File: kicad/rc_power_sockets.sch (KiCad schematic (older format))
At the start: 14 parts

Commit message: Schematic
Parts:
- removed J?: SIL6, symbol SIL6
- added JP?: Jumper_NO_Small, symbol Jumper_NO_Small
- added P?: ICSP, symbol DIL6
- J?: value SIL3 -> Motion Sensor
- J?: value SIL3 -> Radio 433MHZ
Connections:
- net labels added: DATA, MISO, MOSI, RESET, SCK
- net labels removed: MOTION
- wire segments 17 -> 38
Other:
- moved on the sheet: C?, D?, IC?, J?, Q?, R?, SW?, U?

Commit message: Schematic
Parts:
- removed J?: Motion Sensor, symbol SIL3
- removed J?: Radio 433MHZ, symbol SIL3
- added P?: DIL6, symbol DIL6
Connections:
- net labels added: POWER, POWER_SWITCHED, RADIO_DATA
- net labels removed: BATTERY, DATA
- wire segments 38 -> 45
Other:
- moved on the sheet: C?, D?, IC?, JP?, P?, Q?, R?, SW?, U?

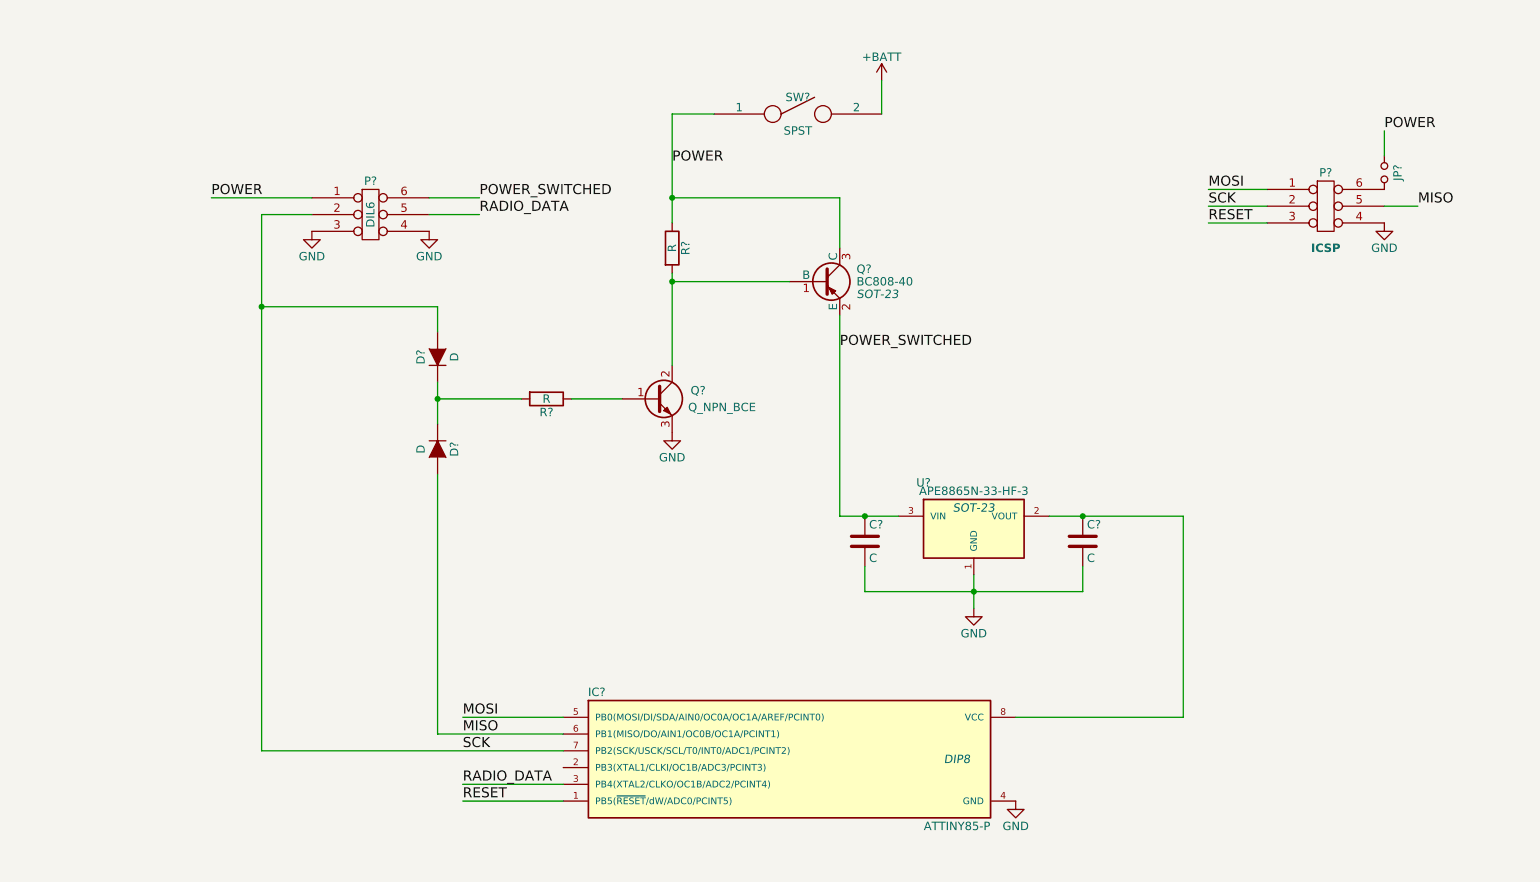
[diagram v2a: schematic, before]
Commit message: SIL for sensors
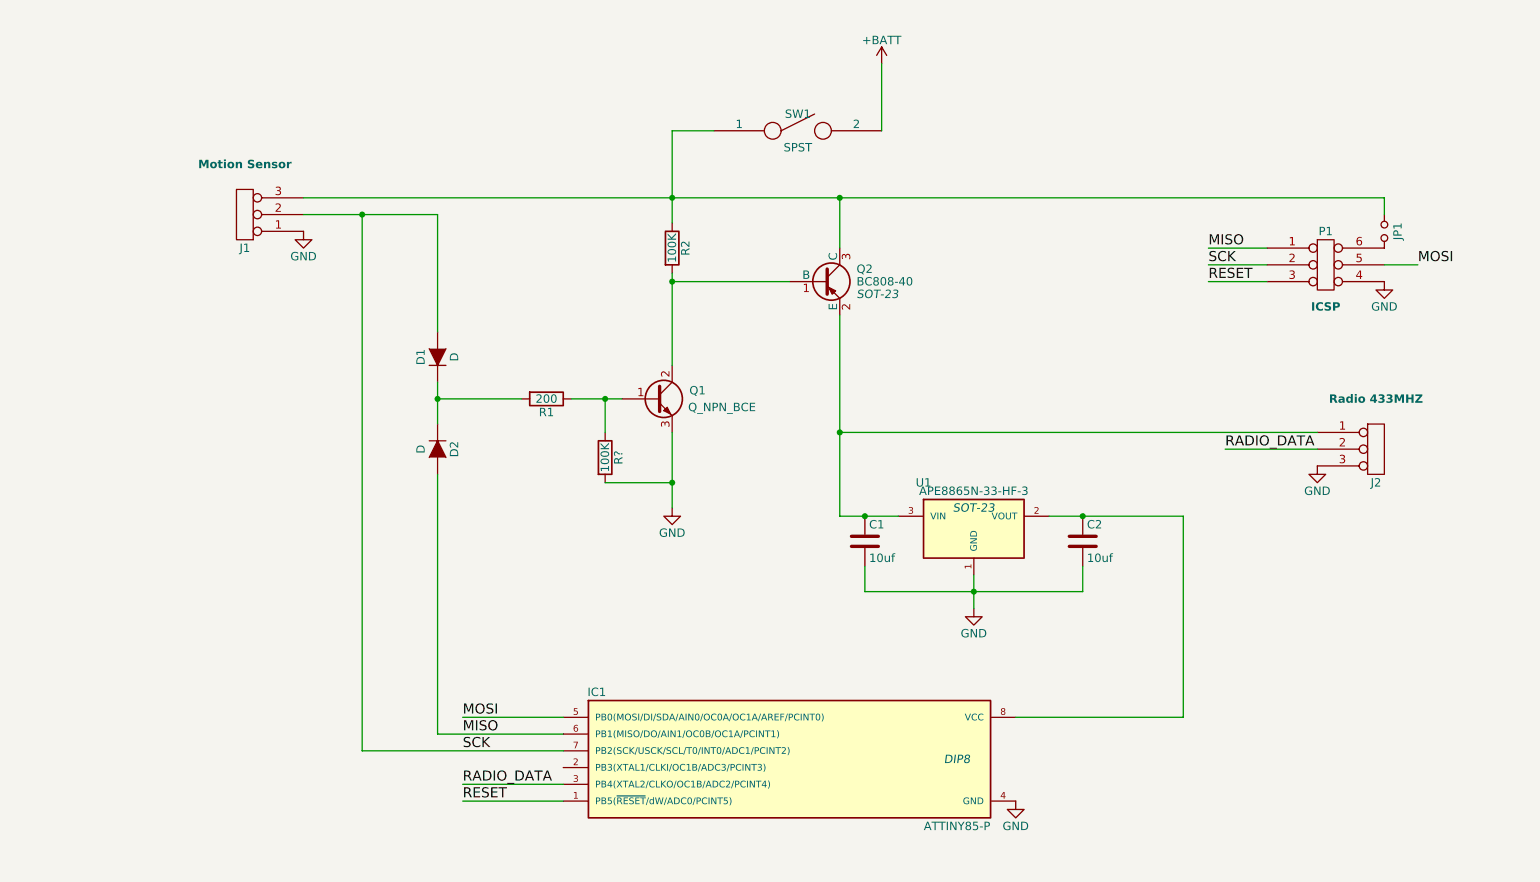
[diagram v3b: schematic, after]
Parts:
- removed P?: DIL6, symbol DIL6
- added J1: Motion Sensor, symbol SIL3
- added J2: Radio 433MHZ, symbol SIL3
- added R?: 100K, symbol R
- C1, C2: renamed from C?; value C -> 10uf
- R1: renamed from R?; value R -> 200
- R2: renamed from R?; value R -> 100K
- gave numbers to parts that had none: 9
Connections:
- net GND: now also J1.1, J2.3, R?.2
- net MISO: now also P1.1 (P1); no longer P1.5 (P5)
- net MOSI: now also P1.5 (P5); no longer P1.1 (P1)
- net RADIO_DATA: now also J2.2
- net SCK: now also J1.2
- net at Q1.1 (B), R1.1: now also R?.1
- net POWER: no longer names the net of JP1.1, Q2.3 (C), R2.1, SW1.1
- net POWER: now also J1.3
- net POWER_SWITCHED: no longer names the net of C1.1, Q2.2 (E), U1.3 (VIN)
- net POWER_SWITCHED: now also J2.1
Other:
- moved on the sheet: JP1, P1, SW1

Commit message: Annotate
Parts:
- added R4: 100K, symbol R
- gave numbers to parts that had none: 1
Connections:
- net RESET: now also R4.1
- net at C2.1, IC1.8 (VCC), U1.2 (VOUT): now also R4.2
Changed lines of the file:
@@
 $EndComp
 $Comp
-L +BATT #PWR3
+L +BATT #PWR01
 U 1 1 56D4AEA2
 P 6800 1150
-F 0 "#PWR3" H 6800 1000 50  0001 C CNN
+F 0 "#PWR01" H 6800 1000 50  0001 C CNN
 F 1 "+BATT" H 6800 1290 50  0000 C CNN
 F 2 "" H 6800 1150 50  0000 C CNN
@@
 $EndComp
 $Comp
-L GND #PWR4
+L GND #PWR02
 U 1 1 56D4B298
 P 7350 4400
-F 0 "#PWR4" H 7350 4150 50  0001 C CNN
+F 0 "#PWR02" H 7350 4150 50  0001 C CNN
 F 1 "GND" H 7350 4250 50  0000 C CNN
 F 2 "" H 7350 4400 50  0000 C CNN
@@
 $EndComp
 $Comp
-L GND #PWR2
+L GND #PWR03
 U 1 1 56D4D563
 P 5550 3800
-F 0 "#PWR2" H 5550 3550 50  0001 C CNN
+F 0 "#PWR03" H 5550 3550 50  0001 C CNN
 F 1 "GND" H 5550 3650 50  0000 C CNN
 F 2 "" H 5550 3800 50  0000 C CNN
@@
 $EndComp
 $Comp
-L GND #PWR5
+L GND #PWR04
 U 1 1 56D4E393
 P 7600 5550
-F 0 "#PWR5" H 7600 5300 50  0001 C CNN
+F 0 "#PWR04" H 7600 5300 50  0001 C CNN
 F 1 "GND" H 7600 5400 50  0000 C CNN
 F 2 "" H 7600 5550 50  0000 C CNN
@@
 SCK
 $Comp
-L GND #PWR7
+L GND #PWR05
 U 1 1 56D7102B
 P 9800 2450
-F 0 "#PWR7" H 9800 2200 50  0001 C CNN
+F 0 "#PWR05" H 9800 2200 50  0001 C CNN
 F 1 "GND" H 9800 2300 50  0000 C CNN
 F 2 "" H 9800 2450 50  0000 C CNN
@@
 RADIO_DATA
 $Comp
-L GND #PWR6
+L GND #PWR06
 U 1 1 56D83AA4
 P 9400 3550
-F 0 "#PWR6" H 9400 3300 50  0001 C CNN
+F 0 "#PWR06" H 9400 3300 50  0001 C CNN
 F 1 "GND" H 9400 3400 50  0000 C CNN
 F 2 "" H 9400 3550 50  0000 C CNN
@@
 $EndComp
 $Comp
-L GND #PWR1
+L GND #PWR07
 U 1 1 56D83C01
 P 3350 2150
-F 0 "#PWR1" H 3350 1900 50  0001 C CNN
+F 0 "#PWR07" H 3350 1900 50  0001 C CNN
 F 1 "GND" H 3350 2000 50  0000 C CNN
 F 2 "" H 3350 2150 50  0000 C CNN
@@
 	8000 4300 8000 4150
 Wire Wire Line
-	8600 3850 8600 5050
+	8600 3850 8600 5950
 Wire Wire Line
 	8600 5050 7600 5050
@@
 	5550 3350 5550 3800
 $Comp
-L R R?
+L R R3
 U 1 1 56D8549B
 P 5150 3500
-F 0 "R?" V 5230 3500 50  0000 C CNN
+F 0 "R3" V 5230 3500 50  0000 C CNN
 F 1 "100K" V 5150 3500 50  0000 C CNN
 F 2 "" V 5080 3500 50  0000 C CNN
@@
 	5150 3350 5150 3150
 Connection ~ 5150 3150
+$Comp
+L R R4
+U 1 1 56D85890
+P 4750 5800
+F 0 "R4" V 4830 5800 50  0000 C CNN
+F 1 "100K" V 4750 5800 50  0000 C CNN
+F 2 "" V 4680 5800 50  0000 C CNN
+F 3 "" H 4750 5800 50  0000 C CNN
+	1    4750 5800
+	1    0    0    -1
+$EndComp
+Wire Wire Line
+	4750 5650 4750 5550
+Connection ~ 4750 5550
+Wire Wire Line
+	8600 5950 4750 5950
+Connection ~ 8600 5050
 $EndSCHEMATC

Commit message: Footprints
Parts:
- C1, C2: footprint (none) -> Capacitors_SMD:C_1206_HandSoldering
- D1, D2: footprint (none) -> SMD_Packages:SMD-1206_Pol
- IC1: footprint DIP8 -> Housings_DIP:DIP-8_W7.62mm_LongPads
- J1, J2: footprint (none) -> Pin_Headers:Pin_Header_Straight_1x03
- JP1: footprint (none) -> Pin_Headers:Pin_Header_Straight_1x02
- P1: footprint (none) -> Pin_Headers:Pin_Header_Straight_2x03
- Q1: footprint (none) -> TO_SOT_Packages_SMD:SOT-23_Handsoldering
- Q2, U1: footprint SOT-23 -> TO_SOT_Packages_SMD:SOT-23_Handsoldering
- R1, R2, R3, R4: footprint (none) -> Resistors_SMD:R_1206_HandSoldering
- SW1: footprint (none) -> Wire_Pads:SolderWirePad_2x_2-5mmDrill
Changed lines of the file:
@@
 F 0 "IC1" H 5100 5700 50  0000 C CNN
 F 1 "ATTINY85-P" H 7250 4900 50  0000 C CNN
-F 2 "DIP8" H 7250 5300 50  0000 C CIN
+F 2 "Housings_DIP:DIP-8_W7.62mm_LongPads" H 7250 5300 50  0000 C CIN
 F 3 "" H 6250 5300 50  0000 C CNN
 	1    6250 5300
@@
 F 0 "Q2" H 6650 2525 50  0000 L CNN
 F 1 "BC808-40" H 6650 2450 50  0000 L CNN
-F 2 "SOT-23" H 6650 2375 50  0000 L CIN
+F 2 "TO_SOT_Packages_SMD:SOT-23_Handsoldering" H 6650 2375 50  0000 L CIN
 F 3 "" H 6450 2450 50  0000 L CNN
 	1    6450 2450
@@
 F 0 "Q1" H 5750 3200 50  0000 R CNN
 F 1 "Q_NPN_BCE" H 6050 3100 50  0000 R CNN
-F 2 "" H 5650 3250 50  0000 C CNN
+F 2 "TO_SOT_Packages_SMD:SOT-23_Handsoldering" H 5650 3250 50  0001 C CNN
 F 3 "" H 5450 3150 50  0000 C CNN
 	1    5450 3150
@@
 F 0 "SW1" H 6300 1650 50  0000 C CNN
 F 1 "SPST" H 6300 1450 50  0000 C CNN
-F 2 "" H 6300 1550 50  0000 C CNN
+F 2 "Wire_Pads:SolderWirePad_2x_2-5mmDrill" H 6300 1550 50  0001 C CNN
 F 3 "" H 6300 1550 50  0000 C CNN
 	1    6300 1550
@@
 F 0 "R1" V 4880 3150 50  0000 C CNN
 F 1 "200" V 4800 3150 50  0000 C CNN
-F 2 "" V 4730 3150 50  0000 C CNN
+F 2 "Resistors_SMD:R_1206_HandSoldering" V 4730 3150 50  0001 C CNN
 F 3 "" H 4800 3150 50  0000 C CNN
 	1    4800 3150
@@
 F 0 "R2" V 5630 2250 50  0000 C CNN
 F 1 "100K" V 5550 2250 50  0000 C CNN
-F 2 "" V 5480 2250 50  0000 C CNN
+F 2 "Resistors_SMD:R_1206_HandSoldering" V 5480 2250 50  0001 C CNN
 F 3 "" H 5550 2250 50  0000 C CNN
 	1    5550 2250
@@
 F 0 "C2" H 8025 4100 50  0000 L CNN
 F 1 "10uf" H 8025 3900 50  0000 L CNN
-F 2 "" H 8038 3850 50  0000 C CNN
+F 2 "Capacitors_SMD:C_1206_HandSoldering" H 8038 3850 50  0001 C CNN
 F 3 "" H 8000 4000 50  0000 C CNN
 	1    8000 4000
@@
 F 0 "U1" H 7050 4150 50  0000 C CNN
 F 1 "APE8865N-33-HF-3" H 7350 4100 50  0000 C CNN
-F 2 "SOT-23" H 7350 4000 50  0000 C CIN
+F 2 "TO_SOT_Packages_SMD:SOT-23_Handsoldering" H 7350 4000 50  0000 C CIN
 F 3 "" H 7350 3900 50  0000 C CNN
 	1    7350 3900
@@
 F 0 "C1" H 6725 4100 50  0000 L CNN
 F 1 "10uf" H 6725 3900 50  0000 L CNN
-F 2 "" H 6738 3850 50  0000 C CNN
+F 2 "Capacitors_SMD:C_1206_HandSoldering" H 6738 3850 50  0001 C CNN
 F 3 "" H 6700 4000 50  0000 C CNN
 	1    6700 4000
@@
 F 0 "D1" H 4150 3000 50  0000 C CNN
 F 1 "D" H 4150 2800 50  0000 C CNN
-F 2 "" H 4150 2900 50  0000 C CNN
+F 2 "SMD_Packages:SMD-1206_Pol" H 4150 2900 50  0001 C CNN
 F 3 "" H 4150 2900 50  0000 C CNN
 	1    4150 2900
@@
 F 0 "D2" H 4150 3550 50  0000 C CNN
 F 1 "D" H 4150 3350 50  0000 C CNN
-F 2 "" H 4150 3450 50  0000 C CNN
+F 2 "SMD_Packages:SMD-1206_Pol" H 4150 3450 50  0001 C CNN
 F 3 "" H 4150 3450 50  0000 C CNN
 	1    4150 3450
@@
 F 0 "P1" H 9450 2550 50  0000 C CNN
 F 1 "ICSP" H 9450 2100 50  0000 C CNB
-F 2 "" H 9450 2350 50  0000 C CNN
+F 2 "Pin_Headers:Pin_Header_Straight_2x03" H 9450 2350 50  0001 C CNN
 F 3 "" H 9450 2350 50  0000 C CNN
 	1    9450 2350
@@
 F 0 "JP1" H 9800 2230 50  0000 C CNN
 F 1 "Jumper_NO_Small" H 9810 2090 50  0001 C CNN
-F 2 "" H 9800 2150 50  0000 C CNN
+F 2 "Pin_Headers:Pin_Header_Straight_1x02" H 9800 2150 50  0001 C CNN
 F 3 "" H 9800 2150 50  0000 C CNN
 	1    9800 2150
@@
 F 0 "J1" H 3000 2250 50  0000 C CNN
 F 1 "Motion Sensor" H 3000 1750 50  0000 C CNB
-F 2 "" H 3050 2050 50  0000 C CNN
+F 2 "Pin_Headers:Pin_Header_Straight_1x03" H 3050 2050 50  0001 C CNN
 F 3 "" H 3050 2050 50  0000 C CNN
 	1    3000 2050
@@
 F 0 "J2" H 9750 3250 50  0000 C CNN
 F 1 "Radio 433MHZ" H 9750 3750 50  0000 C CNB
-F 2 "" H 9800 3450 50  0000 C CNN
+F 2 "Pin_Headers:Pin_Header_Straight_1x03" H 9800 3450 50  0001 C CNN
 F 3 "" H 9800 3450 50  0000 C CNN
 	1    9750 3450
@@
 F 0 "R3" V 5230 3500 50  0000 C CNN
 F 1 "100K" V 5150 3500 50  0000 C CNN
-F 2 "" V 5080 3500 50  0000 C CNN
+F 2 "Resistors_SMD:R_1206_HandSoldering" V 5080 3500 50  0001 C CNN
 F 3 "" H 5150 3500 50  0000 C CNN
 	1    5150 3500
@@
 F 0 "R4" V 4830 5800 50  0000 C CNN
 F 1 "100K" V 4750 5800 50  0000 C CNN
-F 2 "" V 4680 5800 50  0000 C CNN
+F 2 "Resistors_SMD:R_1206_HandSoldering" V 4680 5800 50  0001 C CNN
 F 3 "" H 4750 5800 50  0000 C CNN
 	1    4750 5800

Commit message: Initial pcb
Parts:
- Q1: value Q_NPN_BCE -> N-Channel Mosfet
- Q2: value BC808-40 -> P-Channel Mosfet
- U1: value APE8865N-33-HF-3 -> LDO 3v3 Voltage Regulator
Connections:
- net GND: now also J2.1; no longer J2.3
- net at C1.1, Q2.2 (E), U1.3 (VIN): now also J2.3; no longer J2.1
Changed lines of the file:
@@
 P 6450 2450
 F 0 "Q2" H 6650 2525 50  0000 L CNN
-F 1 "BC808-40" H 6650 2450 50  0000 L CNN
+F 1 "P-Channel Mosfet" H 6650 2450 50  0000 L CNN
 F 2 "TO_SOT_Packages_SMD:SOT-23_Handsoldering" H 6650 2375 50  0000 L CIN
 F 3 "" H 6450 2450 50  0000 L CNN
@@
 P 5450 3150
 F 0 "Q1" H 5750 3200 50  0000 R CNN
-F 1 "Q_NPN_BCE" H 6050 3100 50  0000 R CNN
+F 1 "N-Channel Mosfet" H 6350 3100 50  0000 R CNN
 F 2 "TO_SOT_Packages_SMD:SOT-23_Handsoldering" H 5650 3250 50  0001 C CNN
 F 3 "" H 5450 3150 50  0000 C CNN
@@
 U 1 1 56D4DF04
 P 7350 3900
-F 0 "U1" H 7050 4150 50  0000 C CNN
-F 1 "APE8865N-33-HF-3" H 7350 4100 50  0000 C CNN
+F 0 "U1" H 7100 3650 50  0000 C CNN
+F 1 "LDO 3v3 Voltage Regulator" H 7350 4100 50  0000 C CNN
 F 2 "TO_SOT_Packages_SMD:SOT-23_Handsoldering" H 7350 4000 50  0000 C CIN
 F 3 "" H 7350 3900 50  0000 C CNN
@@
 F 3 "" H 9800 3450 50  0000 C CNN
 	1    9750 3450
-	1    0    0    -1
+	1    0    0    1
 $EndComp
 Text Label 8850 3450 0    60   ~ 0
@@
 Wire Wire Line
 	5550 1550 5550 2100
-Wire Wire Line
-	9400 3350 6550 3350
 Connection ~ 6550 3350
 Wire Wire Line
@@
 	8600 5950 4750 5950
 Connection ~ 8600 5050
+Wire Wire Line
+	9400 3350 6550 3350
 $EndSCHEMATC

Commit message: SMD ATTiny
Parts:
- removed IC1: ATTINY85-P, Housings_DIP:DIP-8_W7.62mm_LongPads, symbol ATTINY85-P
- removed SW1: SPST, Wire_Pads:SolderWirePad_2x_2-5mmDrill, symbol SPST
- added C3: 0.1uf, Capacitors_SMD:C_1206_HandSoldering, symbol C
- added IC1: ATTINY85-S, SMD_Packages:SOIC-8-N, symbol ATTINY85-S
- added SW1: Power Switch, Buttons_Switches_ThroughHole:SW_Micro_SPST_Angled, symbol SWITCH_INV
- J1, J2: footprint Pin_Headers:Pin_Header_Straight_1x03 -> Socket_Strips:Socket_Strip_Straight_1x03
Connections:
- net +BATT: now also SW1.1
- net GND: now also C3.2, IC1.4 (GND), SW1.3
- net MISO: now also IC1.6 (PB1(MISO/DO/AIN1/OC0B/OC1A/PCINT1))
- net MOSI: now also IC1.5 (PB0(MOSI/DI/SDA/AIN0/OC0A/OC1A/AREF/PCINT0))
- net RADIO_DATA: now also IC1.3 (PB4(XTAL2/CLKO/OC1B/ADC2/PCINT4))
- net RESET: now also IC1.1 (PB5(~RESET~/dW/ADC0/PCINT5))
- net SCK: now also IC1.7 (PB2(SCK/USCK/SCL/T0/INT0/ADC1/PCINT2))
- net at C2.1, R4.2, U1.2 (VOUT): now also C3.1, IC1.8 (VCC)
- net at J1.3, JP1.1, Q2.3 (C)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: now also SW1.2
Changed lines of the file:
@@
 $EndDescr
-$Comp
-L ATTINY85-P IC1
-U 1 1 56D4ACD7
-P 6250 5300
-F 0 "IC1" H 5100 5700 50  0000 C CNN
-F 1 "ATTINY85-P" H 7250 4900 50  0000 C CNN
-F 2 "Housings_DIP:DIP-8_W7.62mm_LongPads" H 7250 5300 50  0000 C CIN
-F 3 "" H 6250 5300 50  0000 C CNN
-	1    6250 5300
-	1    0    0    -1
-$EndComp
 $Comp
 L BC808-40 Q2
@@
 $EndComp
 $Comp
-L SPST SW1
-U 1 1 56D4AE59
-P 6300 1550
-F 0 "SW1" H 6300 1650 50  0000 C CNN
-F 1 "SPST" H 6300 1450 50  0000 C CNN
-F 2 "Wire_Pads:SolderWirePad_2x_2-5mmDrill" H 6300 1550 50  0001 C CNN
-F 3 "" H 6300 1550 50  0000 C CNN
-	1    6300 1550
-	1    0    0    -1
-$EndComp
-$Comp
 L +BATT #PWR01
 U 1 1 56D4AEA2
-P 6800 1150
-F 0 "#PWR01" H 6800 1000 50  0001 C CNN
-F 1 "+BATT" H 6800 1290 50  0000 C CNN
-F 2 "" H 6800 1150 50  0000 C CNN
-F 3 "" H 6800 1150 50  0000 C CNN
-	1    6800 1150
+P 6800 1050
+F 0 "#PWR01" H 6800 900 50  0001 C CNN
+F 1 "+BATT" H 6800 1190 50  0000 C CNN
+F 2 "" H 6800 1050 50  0000 C CNN
+F 3 "" H 6800 1050 50  0000 C CNN
+	1    6800 1050
 	1    0    0    -1
 $EndComp
@@
 F 0 "J1" H 3000 2250 50  0000 C CNN
 F 1 "Motion Sensor" H 3000 1750 50  0000 C CNB
-F 2 "Pin_Headers:Pin_Header_Straight_1x03" H 3050 2050 50  0001 C CNN
+F 2 "Socket_Strips:Socket_Strip_Straight_1x03" H 3050 2050 50  0001 C CNN
 F 3 "" H 3050 2050 50  0000 C CNN
 	1    3000 2050
@@
 F 0 "J2" H 9750 3250 50  0000 C CNN
 F 1 "Radio 433MHZ" H 9750 3750 50  0000 C CNB
-F 2 "Pin_Headers:Pin_Header_Straight_1x03" H 9800 3450 50  0001 C CNN
+F 2 "Socket_Strips:Socket_Strip_Straight_1x03" H 9800 3450 50  0001 C CNN
 F 3 "" H 9800 3450 50  0000 C CNN
 	1    9750 3450
@@
 	9800 2350 10000 2350
 Wire Wire Line
-	6800 1150 6800 1550
+	6800 1050 6800 1450
 Wire Wire Line
 	4900 5450 4300 5450
@@
 Wire Wire Line
 	9400 3350 6550 3350
+$Comp
+L C C3
+U 1 1 56D9DCDE
+P 8250 5350
+F 0 "C3" H 8275 5450 50  0000 L CNN
+F 1 "0.1uf" H 8275 5250 50  0000 L CNN
+F 2 "Capacitors_SMD:C_1206_HandSoldering" H 8288 5200 50  0001 C CNN
+F 3 "" H 8250 5350 50  0000 C CNN
+	1    8250 5350
+	1    0    0    -1
+$EndComp
+Wire Wire Line
+	8250 5200 8250 5050
+Connection ~ 8250 5050
+$Comp
+L GND #PWR08
+U 1 1 56D9DFFD
+P 8250 5500
+F 0 "#PWR08" H 8250 5250 50  0001 C CNN
+F 1 "GND" H 8250 5350 50  0000 C CNN
+F 2 "" H 8250 5500 50  0000 C CNN
+F 3 "" H 8250 5500 50  0000 C CNN
+	1    8250 5500
+	1    0    0    -1
+$EndComp
+$Comp
+L ATTINY85-S IC1
+U 1 1 56D9E1BB
+P 6250 5300
+F 0 "IC1" H 5100 5700 50  0000 C CNN
+F 1 "ATTINY85-S" H 7250 4900 50  0000 C CNN
+F 2 "SMD_Packages:SOIC-8-N" H 7200 5300 50  0000 C CIN
+F 3 "" H 6250 5300 50  0000 C CNN
+	1    6250 5300
+	1    0    0    -1
+$EndComp
+$Comp
+L SWITCH_INV SW1
+U 1 1 56D9E668
+P 6300 1550
+F 0 "SW1" H 6100 1700 50  0000 C CNN
+F 1 "Power Switch" H 6150 1400 50  0000 C CNN
+F 2 "Buttons_Switches_ThroughHole:SW_Micro_SPST_Angled" H 6300 1550 50  0001 C CNN
+F 3 "" H 6300 1550 50  0000 C CNN
+	1    6300 1550
+	1    0    0    -1
+$EndComp
+$Comp
+L GND #PWR09
+U 1 1 56D9E7B6
+P 6800 1650
+F 0 "#PWR09" H 6800 1400 50  0001 C CNN
+F 1 "GND" H 6800 1500 50  0000 C CNN
+F 2 "" H 6800 1650 50  0000 C CNN
+F 3 "" H 6800 1650 50  0000 C CNN
+	1    6800 1650
+	1    0    0    -1
+$EndComp
 $EndSCHEMATC
